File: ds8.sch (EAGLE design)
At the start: 92 parts, among them IC1 TM4C1230C3PM, IC2 TPS77333, Q1 BC850, Q2 BC850, Q3 BC850, U1 LM13700M, U2 LM324, U3 LM324, U4 LM741D, X1 MAB5SH

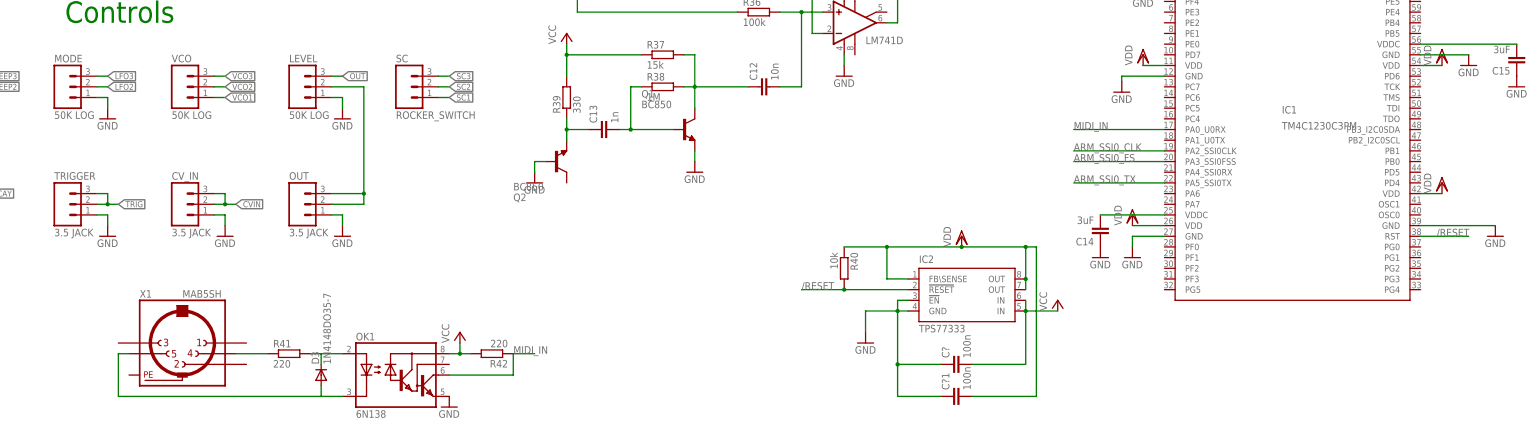
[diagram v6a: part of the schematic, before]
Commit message: added SW debug on midi connector
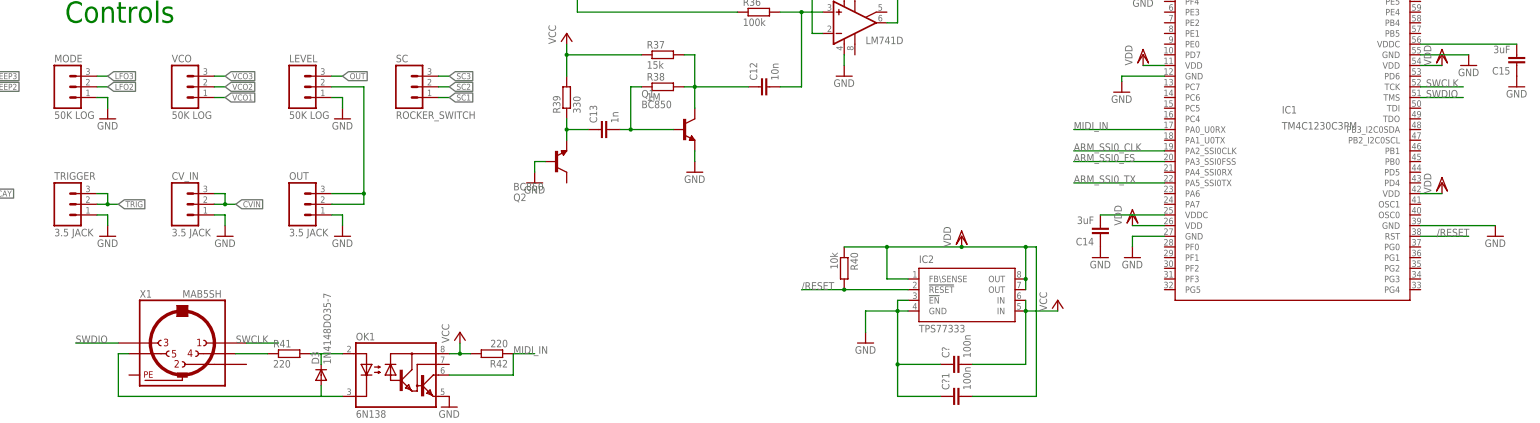
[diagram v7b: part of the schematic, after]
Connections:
- new net SWCLK: IC1.TCK, X1.1
- new net SWDIO: IC1.TMS, X1.3
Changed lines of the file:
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@@
+</segment>
+</net>
+<net name="SWCLK" class="0">
+<segment>
+<pinref part="IC1" gate="G$1" pin="TCK"/>
+<wire x1="325.12" y1="-137.16" x2="335.28" y2="-137.16" width="0.1524" layer="91"/>
+<label x="326.39" y="-137.16" size="1.778" layer="95"/>
+</segment>
+<segment>
+<pinref part="X1" gate="G$1" pin="1"/>
+<wire x1="45.72" y1="-198.12" x2="53.34" y2="-198.12" width="0.1524" layer="91"/>
+<label x="43.18" y="-198.12" size="1.778" layer="95"/>
+</segment>
+</net>
+<net name="SWDIO" class="0">
+<segment>
+<pinref part="IC1" gate="G$1" pin="TMS"/>
+<wire x1="325.12" y1="-139.7" x2="335.28" y2="-139.7" width="0.1524" layer="91"/>
+<label x="326.39" y="-139.7" size="1.778" layer="95"/>
+</segment>
+<segment>
+<pinref part="X1" gate="G$1" pin="3"/>
+<wire x1="15.24" y1="-198.12" x2="5.08" y2="-198.12" width="0.1524" layer="91"/>
+<label x="5.08" y="-198.12" size="1.778" layer="95"/>
 </segment>
 </net>

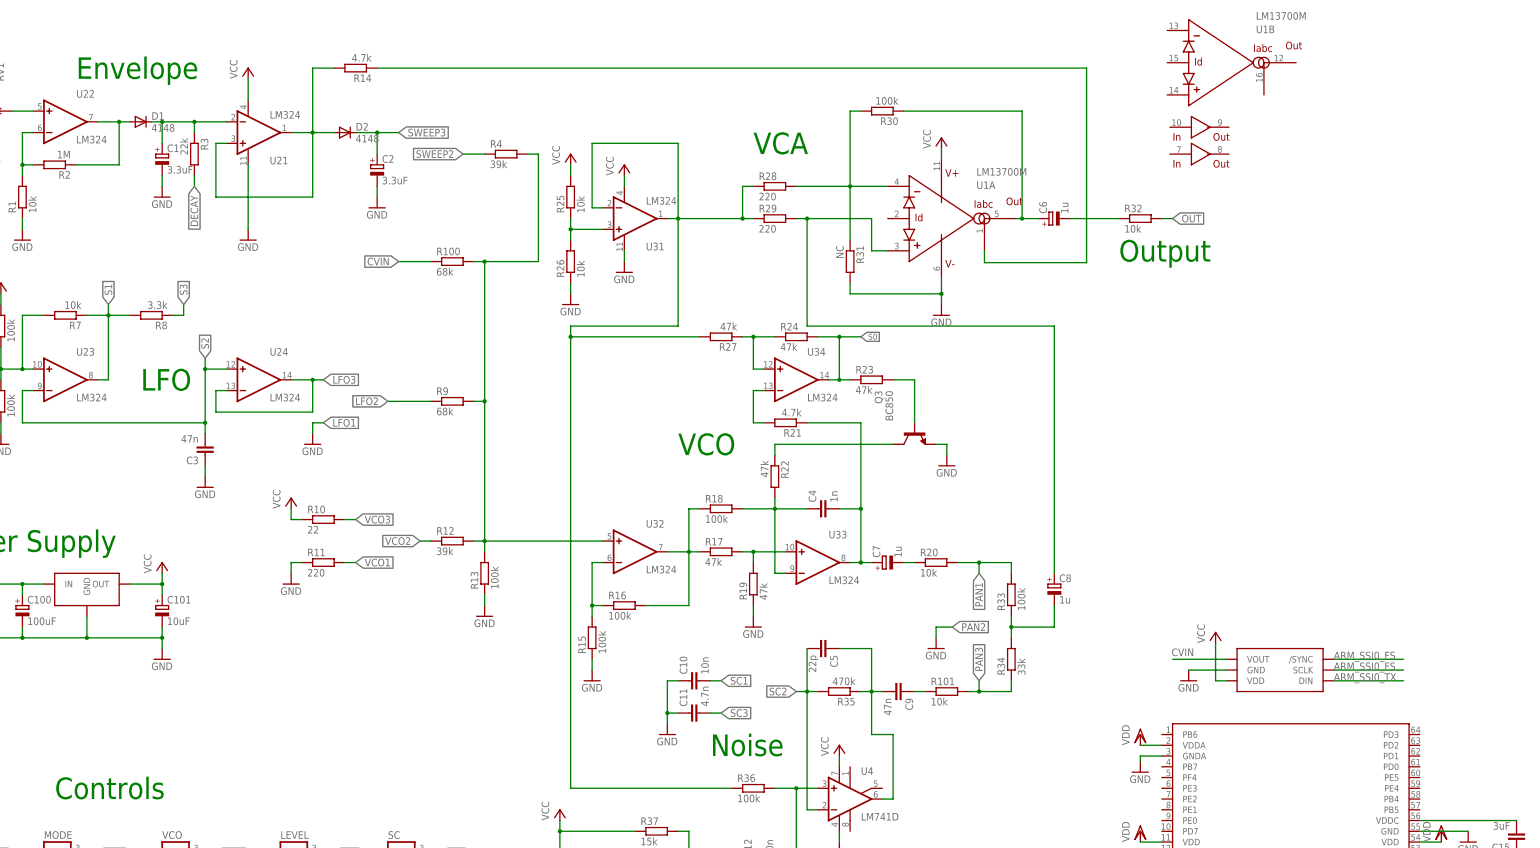
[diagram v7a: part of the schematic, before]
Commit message: added midi trigger
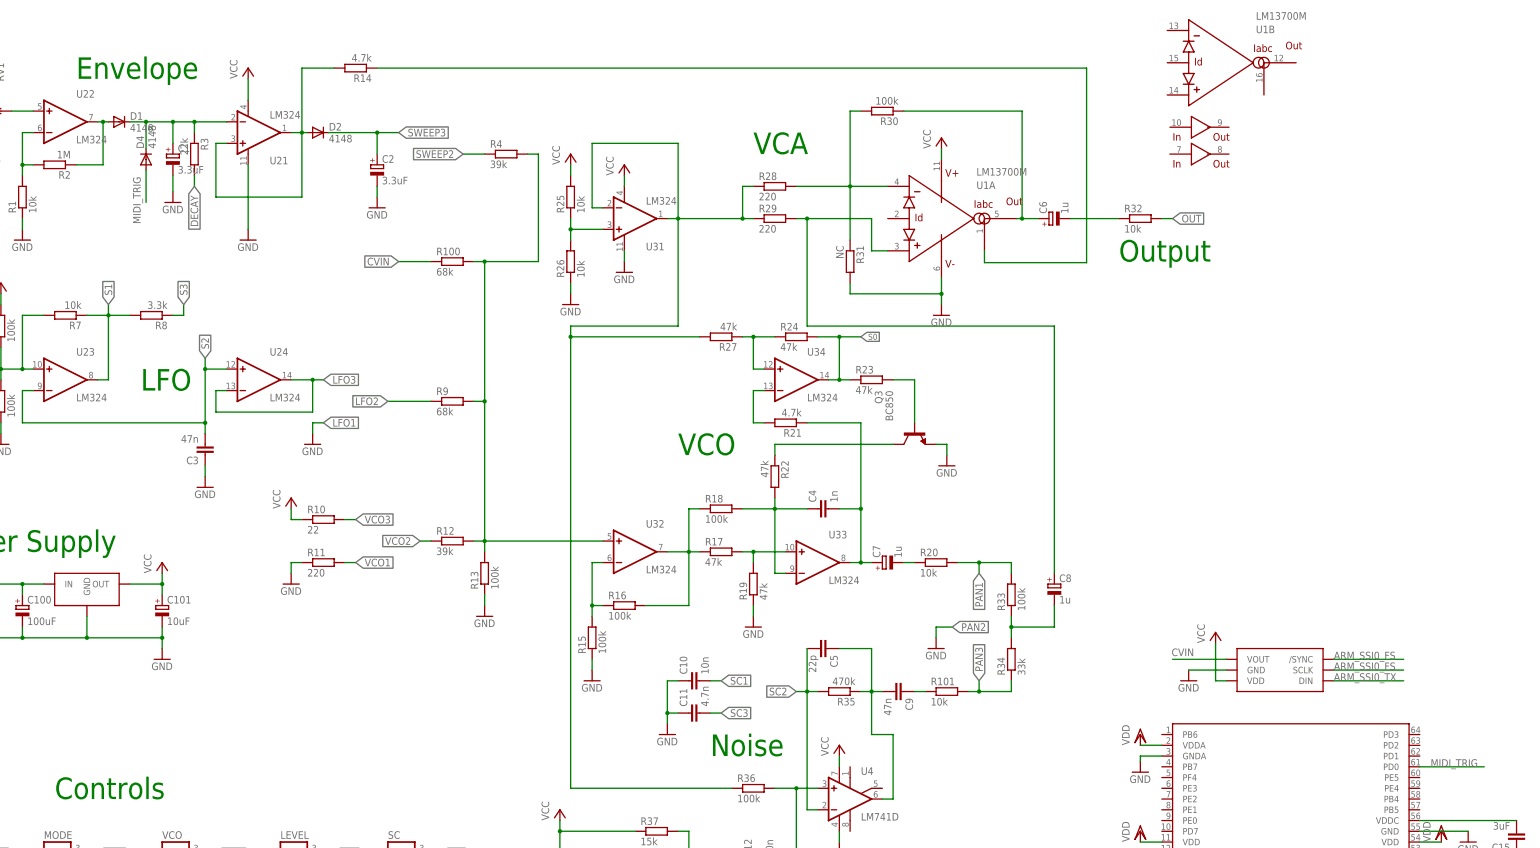
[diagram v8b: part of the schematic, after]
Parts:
- added D4: 4148, diode:DIODE-MINIMELF
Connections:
- new net MIDI_TRIG: D4.A, IC1.PD0
- net N$3: now also D4.C
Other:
- moved on the sheet: C1, D1, D2
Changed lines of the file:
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@@
 <part name="R42" library="rcl" deviceset="R-EU_" device="R0805" value="220"/>
 <part name="GND41" library="supply1" deviceset="GND" device=""/>
+<part name="D4" library="diode" deviceset="DIODE-" device="MINIMELF" value="4148"/>
 </parts>
 <sheets>
@@
 <instance part="GND1" gate="1" x="-5.08" y="10.16"/>
 <instance part="GND2" gate="1" x="48.26" y="10.16"/>
-<instance part="D1" gate="G$1" x="22.86" y="38.1"/>
-<instance part="D2" gate="G$1" x="71.12" y="35.56"/>
+<instance part="D1" gate="G$1" x="17.78" y="38.1"/>
+<instance part="D2" gate="G$1" x="64.77" y="35.56"/>
 <instance part="GND3" gate="1" x="-10.16" y="-38.1"/>
 <instance part="GND4" gate="1" x="58.42" y="-71.12"/>
-<instance part="C1" gate="G$1" x="27.94" y="30.48"/>
+<instance part="C1" gate="G$1" x="30.48" y="30.48"/>
 <instance part="C2" gate="G$1" x="78.74" y="27.94"/>
-<instance part="GND5" gate="1" x="27.94" y="20.32"/>
+<instance part="GND5" gate="1" x="30.48" y="19.05"/>
 <instance part="GND6" gate="1" x="78.74" y="17.78"/>
 <instance part="C101" gate="G$1" x="27.94" y="-76.2"/>
@@
 <instance part="R42" gate="G$1" x="104.14" y="-200.66" rot="R180"/>
 <instance part="GND41" gate="1" x="93.98" y="-213.36"/>
+<instance part="D4" gate="G$1" x="24.13" y="29.21" rot="R90"/>
 </instances>
 <busses>
@@
 <segment>
 <pinref part="U2" gate="2" pin="OUT"/>
-<wire x1="12.7" y1="38.1" x2="17.78" y2="38.1" width="0.1524" layer="91"/>
-<wire x1="17.78" y1="38.1" x2="17.78" y2="27.94" width="0.1524" layer="91"/>
+<wire x1="12.7" y1="38.1" x2="13.97" y2="38.1" width="0.1524" layer="91"/>
+<wire x1="13.97" y1="38.1" x2="13.97" y2="27.94" width="0.1524" layer="91"/>
 <pinref part="R2" gate="G$1" pin="1"/>
-<wire x1="17.78" y1="27.94" x2="7.62" y2="27.94" width="0.1524" layer="91"/>
+<wire x1="13.97" y1="27.94" x2="7.62" y2="27.94" width="0.1524" layer="91"/>
 <pinref part="D1" gate="G$1" pin="A"/>
-<wire x1="20.32" y1="38.1" x2="17.78" y2="38.1" width="0.1524" layer="91"/>
-<junction x="17.78" y="38.1"/>
+<wire x1="15.24" y1="38.1" x2="13.97" y2="38.1" width="0.1524" layer="91"/>
+<junction x="13.97" y="38.1"/>
 </segment>
 </net>
@@
 <wire x1="35.56" y1="38.1" x2="35.56" y2="35.56" width="0.1524" layer="91"/>
 <pinref part="D1" gate="G$1" pin="C"/>
-<wire x1="35.56" y1="38.1" x2="27.94" y2="38.1" width="0.1524" layer="91"/>
-<wire x1="27.94" y1="38.1" x2="25.4" y2="38.1" width="0.1524" layer="91"/>
-<junction x="27.94" y="38.1"/>
+<wire x1="35.56" y1="38.1" x2="30.48" y2="38.1" width="0.1524" layer="91"/>
+<wire x1="30.48" y1="38.1" x2="24.13" y2="38.1" width="0.1524" layer="91"/>
+<junction x="30.48" y="38.1"/>
 <pinref part="C1" gate="G$1" pin="+"/>
-<wire x1="27.94" y1="38.1" x2="27.94" y2="33.02" width="0.1524" layer="91"/>
+<wire x1="24.13" y1="38.1" x2="20.32" y2="38.1" width="0.1524" layer="91"/>
+<wire x1="30.48" y1="38.1" x2="30.48" y2="33.02" width="0.1524" layer="91"/>
 <junction x="35.56" y="38.1"/>
+<pinref part="D4" gate="G$1" pin="C"/>
+<wire x1="24.13" y1="31.75" x2="24.13" y2="38.1" width="0.1524" layer="91"/>
+<junction x="24.13" y="38.1"/>
 </segment>
 </net>
@@
 <wire x1="43.18" y1="33.02" x2="40.64" y2="33.02" width="0.1524" layer="91"/>
 <wire x1="40.64" y1="33.02" x2="40.64" y2="20.32" width="0.1524" layer="91"/>
-<wire x1="40.64" y1="20.32" x2="63.5" y2="20.32" width="0.1524" layer="91"/>
-<wire x1="63.5" y1="20.32" x2="63.5" y2="35.56" width="0.1524" layer="91"/>
+<wire x1="40.64" y1="20.32" x2="60.96" y2="20.32" width="0.1524" layer="91"/>
+<wire x1="60.96" y1="20.32" x2="60.96" y2="35.56" width="0.1524" layer="91"/>
 <pinref part="U2" gate="1" pin="OUT"/>
-<wire x1="63.5" y1="35.56" x2="58.42" y2="35.56" width="0.1524" layer="91"/>
+<wire x1="60.96" y1="35.56" x2="58.42" y2="35.56" width="0.1524" layer="91"/>
 <pinref part="R14" gate="G$1" pin="2"/>
-<wire x1="63.5" y1="35.56" x2="63.5" y2="50.8" width="0.1524" layer="91"/>
-<wire x1="63.5" y1="50.8" x2="68.58" y2="50.8" width="0.1524" layer="91"/>
-<junction x="63.5" y="35.56"/>
+<wire x1="60.96" y1="35.56" x2="60.96" y2="50.8" width="0.1524" layer="91"/>
+<wire x1="60.96" y1="50.8" x2="68.58" y2="50.8" width="0.1524" layer="91"/>
+<junction x="60.96" y="35.56"/>
 <pinref part="D2" gate="G$1" pin="A"/>
-<wire x1="68.58" y1="35.56" x2="63.5" y2="35.56" width="0.1524" layer="91"/>
+<wire x1="62.23" y1="35.56" x2="60.96" y2="35.56" width="0.1524" layer="91"/>
 </segment>
 </net>
@@
 <pinref part="C1" gate="G$1" pin="-"/>
 <pinref part="GND5" gate="1" pin="GND"/>
-<wire x1="27.94" y1="25.4" x2="27.94" y2="22.86" width="0.1524" layer="91"/>
+<wire x1="30.48" y1="25.4" x2="30.48" y2="21.59" width="0.1524" layer="91"/>
 </segment>
 <segment>
@@
 <segment>
 <pinref part="D2" gate="G$1" pin="C"/>
-<wire x1="73.66" y1="35.56" x2="78.74" y2="35.56" width="0.1524" layer="91"/>
+<wire x1="67.31" y1="35.56" x2="78.74" y2="35.56" width="0.1524" layer="91"/>
 <wire x1="78.74" y1="35.56" x2="83.82" y2="35.56" width="0.1524" layer="91"/>
 <label x="83.82" y="35.56" size="1.778" layer="95" xref="yes"/>
@@
 </segment>
 </net>
+<net name="MIDI_TRIG" class="0">
+<segment>
+<pinref part="IC1" gate="G$1" pin="PD0"/>
+<wire x1="325.12" y1="-114.3" x2="340.36" y2="-114.3" width="0.1524" layer="91"/>
+<label x="327.66" y="-114.3" size="1.778" layer="95"/>
+</segment>
+<segment>
+<pinref part="D4" gate="G$1" pin="A"/>
+<wire x1="24.13" y1="26.67" x2="24.13" y2="19.05" width="0.1524" layer="91"/>
+<label x="22.86" y="13.97" size="1.778" layer="95" rot="R90"/>
+</segment>
+</net>
